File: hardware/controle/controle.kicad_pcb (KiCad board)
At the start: 2 copper layers, 97 x 67.8 mm, 79 parts, among them J1 Barrel_Jack, J10 Conn_01x05_Pin, J11 PWM, J12 ADC, J2 Serial, J3 PWR, J4 DATA, J5 UART7, J6 TWI3, J7 SENS0375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

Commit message: Controle: route board
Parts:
- moved R22 23.3 mm to (116.5, 90.0), turned to 0 degrees
- moved R21 23.2 mm to (111.6, 91.3), turned to 90 degrees
- moved R5 17.4 mm to (55.5, 91.0)
- moved R19 9.49 mm to (119.3, 105.2), turned to -90 degrees
- moved R4 9.22 mm to (50.9, 90.0), turned to 0 degrees
- moved C14 9.04 mm to (112.6, 102.7), turned to 90 degrees
- moved C15 6.83 mm to (119.3, 101.1), turned to 90 degrees
- moved C10 4.68 mm to (50.9, 86.0), turned to 0 degrees
- moved C4 3.36 mm to (82.9, 119.3)
- moved C5 3.36 mm to (93.1, 119.3)
- moved U2 3.36 mm to (89.7, 113.5)
- moved C3 3.36 mm to (84.1, 112.6)
- moved Y1 3.36 mm to (88.0, 120.6)
- moved J7 2.04 mm to (121.8, 120.0)
- moved R25 2.04 mm to (114.0, 123.5)
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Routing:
- net +3V3: track 0.00 -> 231.1 mm, vias 0 -> 4
- net +12V: track 0.00 -> 205.7 mm, vias 0 -> 2
- net GND: track 0.00 -> 115.2 mm, vias 0 -> 8
- net /power/+5VCPU: track 0.00 -> 103.0 mm, vias 0 -> 1
- net /PI2/TWI4_SCK: track 0.00 -> 84.0 mm
- net /PI3/TWI4_SDA: track 0.00 -> 73.7 mm
- net /PI15/EINT27: track 0.00 -> 57.2 mm, vias 0 -> 2
- net Net-(U3-VFB): track 0.00 -> 53.1 mm, vias 0 -> 2
- net Net-(D2-BK): track 0.00 -> 43.7 mm, vias 0 -> 1
- net /PI0/TWI3_SCK: track 0.00 -> 42.8 mm, vias 0 -> 2
- net Net-(D3-GK): track 0.00 -> 39.2 mm, vias 0 -> 1
- net Net-(D2-RK): track 0.00 -> 38.2 mm, vias 0 -> 1
- net /PI1/TWI3_SDA: track 0.00 -> 37.4 mm, vias 0 -> 2
- net Net-(D3-BK): track 0.00 -> 35.8 mm, vias 0 -> 1
- net /LIN/LBUS: track 0.00 -> 34.3 mm
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- added copper zone on B.Cu, net GND
- added copper zone on F.Cu, net GND

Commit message: Update LED resistors values. Minor updates to PCB
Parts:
- R10, R11, R12, R13, R14, R15, R16, R17, R18, R7, R8, R9: value 2.2K -> 330
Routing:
- net GND: track 115.2 -> 124.6 mm
- net /PI3/TWI4_SDA: track 73.7 -> 74.6 mm
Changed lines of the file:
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@@
 			)
 		)
-		(property "Value" "2.2K"
+		(property "Value" "330"
 			(at 0 1.65 0)
 			(layer "F.Fab")
@@
 			)
 		)
-		(property "Value" "2.2K"
+		(property "Value" "330"
 			(at 0 1.65 0)
 			(layer "F.Fab")
@@
 			)
 		)
-		(property "Value" "2.2K"
+		(property "Value" "330"
 			(at 0 1.65 0)
 			(layer "F.Fab")
@@
 			)
 		)
-		(property "Value" "2.2K"
+		(property "Value" "330"
 			(at 0 1.65 0)
 			(layer "F.Fab")
@@
 		(sheetname "Root")
 		(sheetfile "controle.kicad_sch")
-		(attr smd)
+		(attr smd dnp)
 		(fp_line
 			(start -0.227064 -0.735)
@@
 			)
 		)
-		(property "Value" "2.2K"
+		(property "Value" "330"
 			(at 0 1.65 0)
 			(layer "F.Fab")
@@
 			)
 		)
-		(property "Value" "2.2K"
+		(property "Value" "330"
 			(at 0 1.65 0)
 			(layer "F.Fab")
@@
 		(sheetname "Root")
 		(sheetfile "controle.kicad_sch")
-		(attr smd)
+		(attr smd dnp)
 		(fp_line
 			(start -0.227064 -0.735)
@@
 			)
 		)
-		(property "Value" "2.2K"
+		(property "Value" "330"
 			(at 0 1.65 0)
 			(layer "F.Fab")
@@
 		(sheetname "Root")
 		(sheetfile "controle.kicad_sch")
-		(attr smd)
+		(attr smd dnp)
 		(fp_line
 			(start -0.227064 -0.735)
@@
 			)
 		)
-		(property "Value" "2.2K"
+		(property "Value" "330"
 			(at 0 1.65 0)
 			(layer "F.Fab")
@@
 		(sheetname "Root")
 		(sheetfile "controle.kicad_sch")
-		(attr smd)
+		(attr smd dnp)
 		(fp_line
 			(start -0.227064 -0.735)
@@
 			)
 		)
-		(property "Value" "2.2K"
+		(property "Value" "330"
 			(at 0 1.65 0)
 			(layer "F.Fab")
@@
 		(sheetname "Root")
 		(sheetfile "controle.kicad_sch")
-		(attr smd)
+		(attr smd dnp)
 		(fp_line
 			(start -0.227064 -0.735)
@@
 		(tags "resistor handsolder")
 		(property "Reference" "R22"
-			(at 0 -1.65 360)
+			(at 0 -1.65 0)
 			(layer "F.SilkS")
 			(effects
@@
 		)
 		(property "Value" "10K"
-			(at 0 1.65 360)
+			(at 0 1.65 0)
 			(layer "F.Fab")
 			(effects
@@
 		)
 		(fp_text user "${REFERENCE}"
-			(at 0 0 360)
+			(at 0 0 0)
 			(layer "F.Fab")
 			(effects
@@
 		(tags "SOT TO_SOT_SMD")
 		(property "Reference" "Q1"
-			(at 0 -2.4 360)
+			(at 0 -2.4 0)
 			(layer "F.SilkS")
 			(effects
@@
 		)
 		(property "Value" "DMG2307L"
-			(at 0 2.4 360)
+			(at 0 2.4 0)
 			(layer "F.Fab")
 			(effects
@@
 		)
 		(fp_text user "${REFERENCE}"
-			(at 0 0 360)
+			(at 0 0 0)
 			(layer "F.Fab")
 			(effects
@@
 			)
 		)
-		(property "Value" "2.2K"
+		(property "Value" "330"
 			(at 0 1.65 0)
 			(layer "F.Fab")
@@
 			)
 		)
-		(property "Value" "2.2K"
+		(property "Value" "330"
 			(at 0 1.65 0)
 			(layer "F.Fab")
@@
 			)
 		)
-		(property "Value" "2.2K"
+		(property "Value" "330"
 			(at 0 1.65 0)
 			(layer "F.Fab")
@@
 		(sheetname "Root")
 		(sheetfile "controle.kicad_sch")
-		(attr smd)
+		(attr smd dnp)
 		(fp_line
 			(start -0.227064 -0.735)
@@
 	)
 	(segment
+		(start 105.918 103.8084)
+		(end 105.9324 103.8228)
+		(width 0.2)
+		(layer "F.Cu")
+		(net 2)
+	)
+	(segment
 		(start 103.6828 90.932)
 		(end 103.6828 89.679118)
@@
 	)
 	(segment
+		(start 105.918 103.8084)
+		(end 102.1856 103.8084)
+		(width 0.2)
+		(layer "F.Cu")
+		(net 2)
+	)
+	(segment
 		(start 103.6828 93.0556)
 		(end 103.6828 90.932)
@@
 	)
 	(segment
-		(start 109.1424 103.8084)
-		(end 102.1856 103.8084)
+		(start 105.9324 106.9484)
+		(end 110.363 111.379)
 		(width 0.2)
 		(layer "F.Cu")
@@
 	)
 	(segment
+		(start 109.1424 103.8084)
+		(end 105.918 103.8084)
+		(width 0.2)
+		(layer "F.Cu")
+		(net 2)
+	)
+	(segment
 		(start 92.3438 93.679348)
 		(end 93.599 92.424148)
@@
 		(net 2)
 	)
+	(segment
+		(start 105.9324 103.8228)
+		(end 105.9324 106.9484)
+		(width 0.2)
+		(layer "F.Cu")
+		(net 2)
+	)
 	(via
 		(at 124.968 125.222)
@@
 	(segment
 		(start 104.0624 105.5784)
-		(end 104.0624 106.553399)
+		(end 104.0624 106.2214)
 		(width 0.5)
 		(layer "F.Cu")
@@
 	)
 	(segment
-		(start 102.01 112.551)
-		(end 102.01 119.966001)
+		(start 89.764 100.305)
+		(end 100.203 110.744)
 		(width 0.5)
 		(layer "F.Cu")
@@
 	)
 	(segment
-		(start 124.3584 120.576799)
-		(end 122.405599 122.5296)
+		(start 104.0624 106.2214)
+		(end 115.316 117.475)
 		(width 0.5)
 		(layer "F.Cu")
@@
 	)
 	(segment
-		(start 89.764 100.305)
-		(end 102.01 112.551)
+		(start 100.203 118.159001)
+		(end 104.624399 122.5804)
 		(width 0.5)
 		(layer "F.Cu")
@@
 	)
 	(segment
-		(start 102.01 119.966001)
-		(end 104.624399 122.5804)
+		(start 100.203 110.744)
+		(end 100.203 118.159001)
+		(width 0.5)
+		(layer "F.Cu")
+		(net 52)
+	)
+	(segment
+		(start 104.624399 122.5804)
+		(end 105.945199 122.5804)
 		(width 0.5)
 		(layer "F.Cu")
@@
 	)
 	(segment
-		(start 104.624399 122.5804)
-		(end 105.945199 122.5804)
-		(width 0.5)
+		(start 114.022399 122.5296)
+		(end 105.995999 122.5296)
+		(width 0.4)
 		(layer "F.Cu")
 		(net 52)
 	)
 	(segment
-		(start 104.0624 106.553399)
-		(end 114.984001 117.475)
+		(start 124.3584 120.576799)
+		(end 122.405599 122.5296)
 		(width 0.5)
 		(layer "F.Cu")
@@
 	)
 	(segment
-		(start 114.022399 122.5296)
-		(end 105.995999 122.5296)
-		(width 0.4)
+		(start 115.316 117.475)
+		(end 122.430999 117.475)
+		(width 0.5)
 		(layer "F.Cu")
 		(net 52)
@@
 	)
 	(segment
-		(start 114.984001 117.475)
-		(end 122.430999 117.475)
-		(width 0.5)
-		(layer "F.Cu")
-		(net 52)
-	)
-	(segment
 		(start 67.3404 88.2824)
 		(end 66.2004 87.1424)
@@
 	)
 	(segment
-		(start 116.332 120.0404)
-		(end 102.7924 106.5008)
+		(start 90.399 99.035)
+		(end 101.219 109.855)
 		(width 0.5)
 		(layer "F.Cu")
@@
 	)
 	(segment
-		(start 81.837 99.035)
-		(end 90.399 99.035)
+		(start 102.7924 106.136084)
+		(end 102.7924 105.5784)
+		(width 0.5)
+		(layer "F.Cu")
+		(net 56)
+	)
+	(segment
+		(start 104.1654 120.0404)
+		(end 105.945199 120.0404)
 		(width 0.5)
 		(layer "F.Cu")
@@
 	)
 	(segment
-		(start 102.71 111.346)
-		(end 102.71 114.109138)
+		(start 116.586 120.0404)
+		(end 116.586 119.929684)
 		(width 0.5)
 		(layer "F.Cu")
@@
 	)
 	(segment
-		(start 116.586 120.0404)
-		(end 116.332 120.0404)
+		(start 81.837 99.035)
+		(end 90.399 99.035)
 		(width 0.5)
 		(layer "F.Cu")
@@
 	)
 	(segment
-		(start 102.7924 106.5008)
-		(end 102.7924 105.5784)
+		(start 101.219 109.855)
+		(end 101.219 117.094)
 		(width 0.5)
 		(layer "F.Cu")
@@
 	)
 	(segment
-		(start 117.730799 120.0912)
-		(end 117.679999 120.0404)
+		(start 116.586 119.929684)
+		(end 102.7924 106.136084)
 		(width 0.5)
 		(layer "F.Cu")
@@
 	)
 	(segment
-		(start 102.71 114.109138)
-		(end 105.945199 117.344337)
+		(start 117.730799 120.0912)
+		(end 117.679999 120.0404)
 		(width 0.5)
 		(layer "F.Cu")
@@
 	)
 	(segment
-		(start 105.945199 117.344337)
-		(end 105.945199 120.0404)
+		(start 101.219 117.094)
+		(end 104.1654 120.0404)
 		(width 0.5)
 		(layer "F.Cu")
@@
 		(width 0.5)
 		(layer "F.Cu")
-		(net 56)
-	)
-	(segment
-		(start 90.399 99.035)
-		(end 102.71 111.346)
-		(width 0.5)
-		(layer "F.Cu")

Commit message: controle: minor board update
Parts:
- moved R6 1.98 mm to (115.4, 70.8), turned to -90 degrees
- moved D1 1.81 mm to (111.6, 71.8), turned to -90 degrees
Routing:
- net /LIN/LBUS: track 34.3 -> 30.7 mm

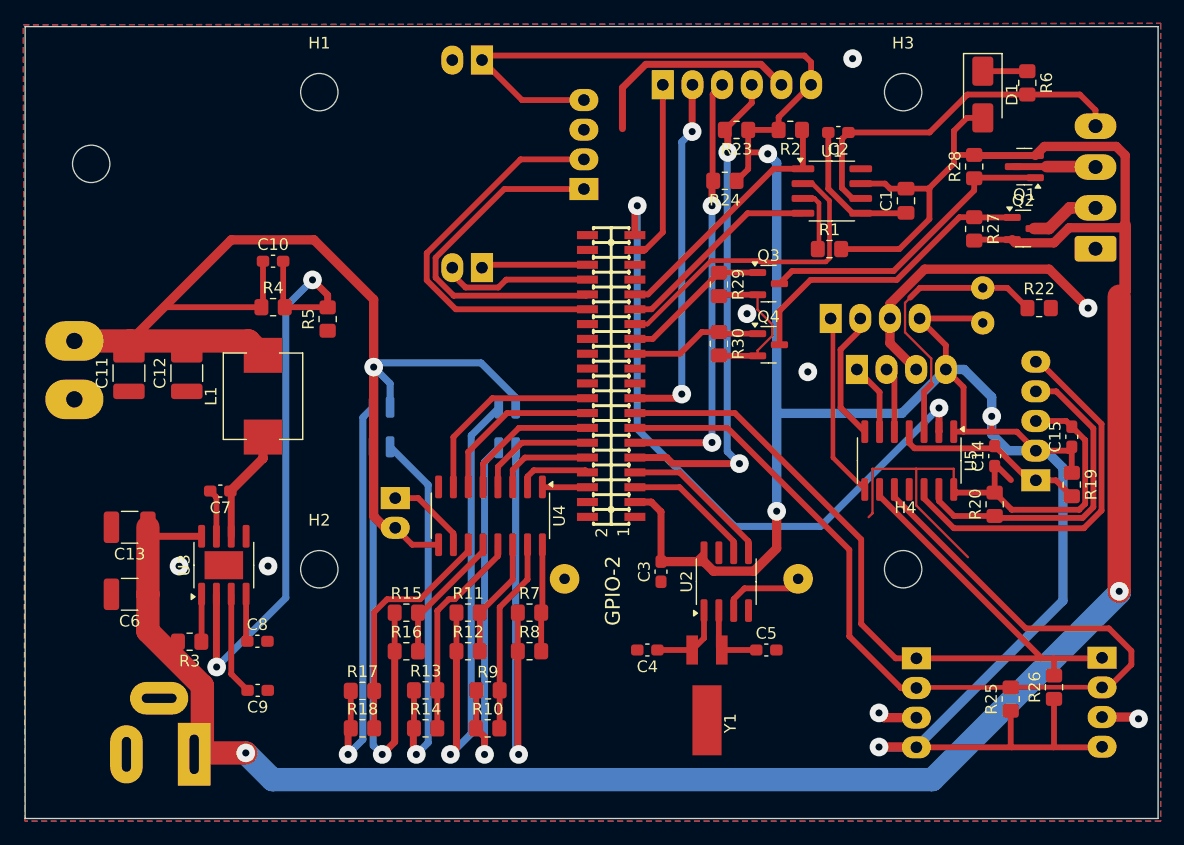
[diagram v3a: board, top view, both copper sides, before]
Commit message: controle: - add leds for LIN power - add optional led for LIN activity - fix lime2 mounting holes - other misc cleanups
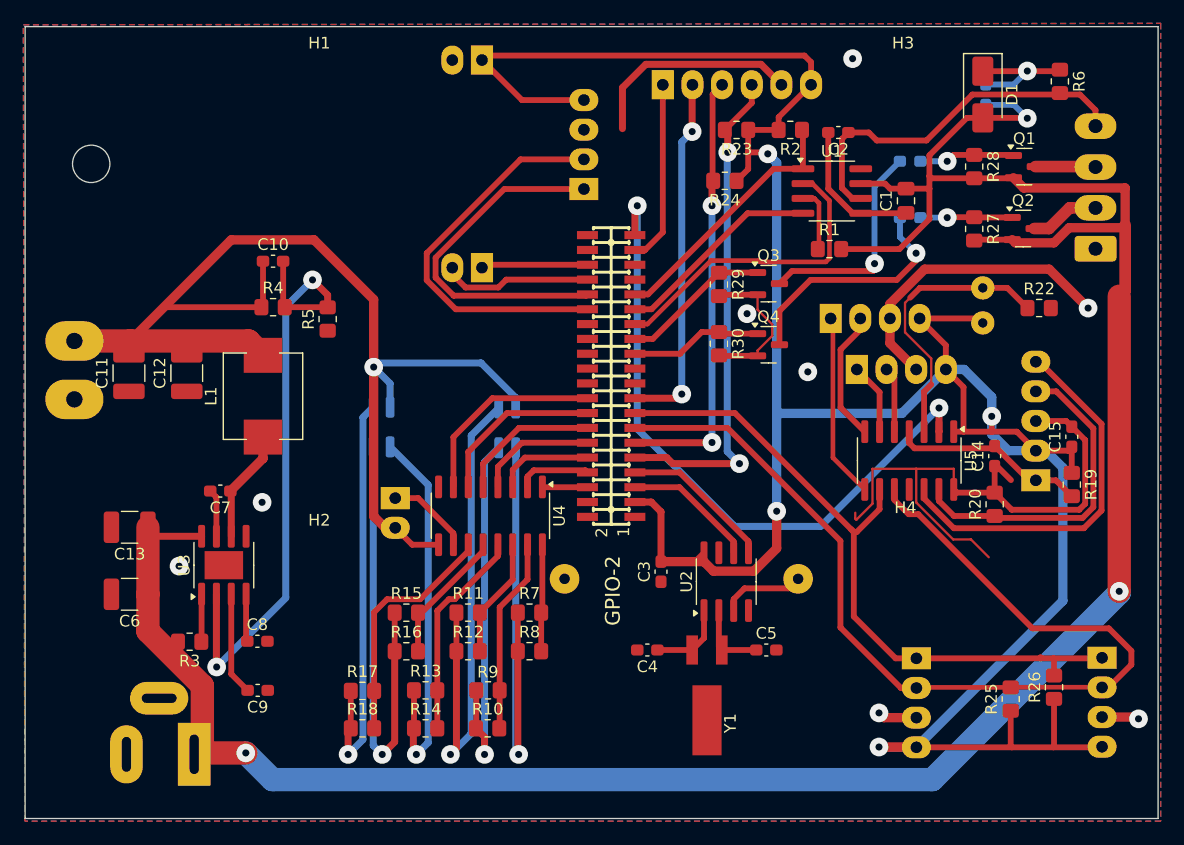
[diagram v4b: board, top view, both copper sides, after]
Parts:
- added D4: RED, LED_SMD:LED_0603_1608Metric_Pad1.05x0.95mm_HandSolder, B.Cu at (105.4, 77.5)
- added D5: RED, LED_SMD:LED_0603_1608Metric_Pad1.05x0.95mm_HandSolder, B.Cu at (105.4, 82.3)
- added D6: RED, LED_SMD:LED_0603_1608Metric_Pad1.05x0.95mm_HandSolder, B.Cu at (111.9, 71.8)
- R27, R28: value 47K -> 2.2K
- moved R6 2.80 mm to (118.2, 70.6)
- turned Q1 to 0 degrees
- turned R28 to -90 degrees
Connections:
- Q1 pad 1: Net-(Q1-G) -> Net-(D4-A)
- Q2 pad 1: Net-(Q2-G) -> Net-(D5-A)
- Q3 pad 3: Net-(Q1-G) -> Net-(D4-K)
- Q4 pad 3: Net-(Q2-G) -> Net-(D5-K)
- R27 pad 1: Net-(Q2-G) -> Net-(D5-A)
- R28 pad 1: Net-(Q1-G) -> Net-(D4-A)
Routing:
- net Net-(Q1-G): track 26.2 -> 0.00 mm
- net Net-(Q2-G): track 26.1 -> 0.00 mm
- net Net-(D5-K): track 0.00 -> 20.6 mm, vias 0 -> 1
- net Net-(D4-K): track 0.00 -> 18.8 mm, vias 0 -> 1
- net /PI3/TWI4_SDA: track 74.6 -> 59.6 mm
- net Net-(D4-A): track 0.00 -> 8.14 mm, vias 0 -> 1
- net Net-(D5-A): track 0.00 -> 7.86 mm, vias 0 -> 1
- net +12V: track 205.8 -> 212.8 mm, vias 2 -> 3
- net Net-(D1-K): track 3.81 -> 10.5 mm, vias 0 -> 1
- net GND: track 124.6 -> 127.5 mm
- net /LIN/+12V1: track 7.00 -> 5.12 mm
- net /LIN/LBUS: track 30.7 -> 31.2 mm

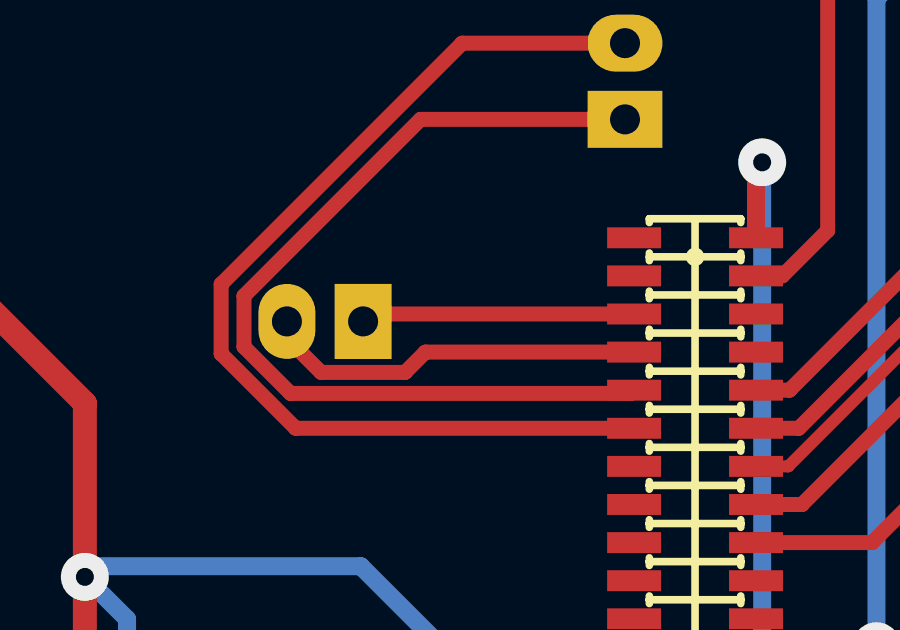
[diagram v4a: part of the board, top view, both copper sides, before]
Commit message: controle: fix orioentation of rs232 module connector
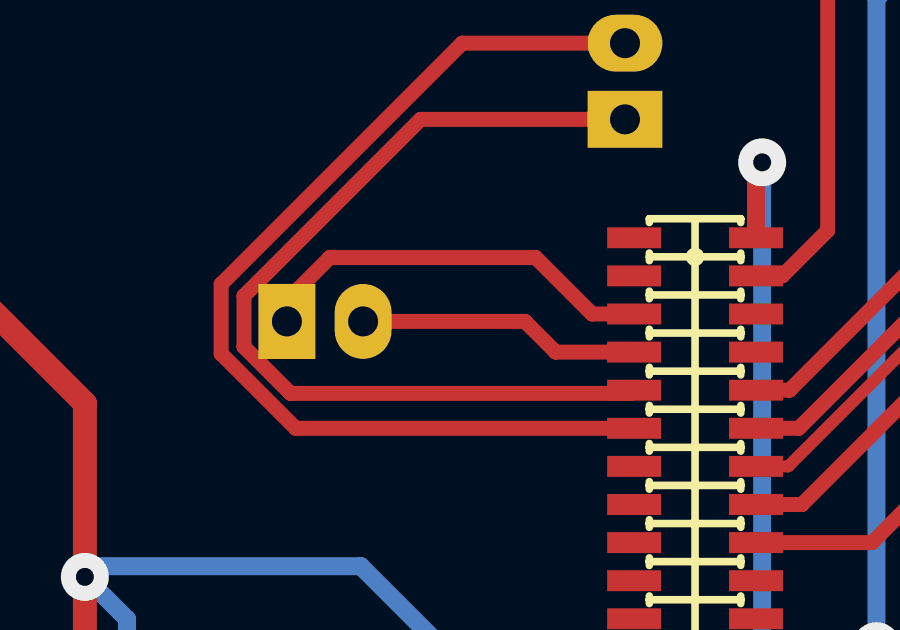
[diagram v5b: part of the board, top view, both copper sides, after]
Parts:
- moved J4 2.54 mm to (66.2, 86.6), turned to -90 degrees
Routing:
- net /PI18/UART2_TX: track 8.79 -> 13.6 mm
- net /PI19/UART2_RX: track 12.3 -> 9.46 mm
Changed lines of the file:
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@@
 		(tags "SOT TO_SOT_SMD")
 		(property "Reference" "Q1"
-			(at 0 -2.4 360)
+			(at 0 -2.4 0)
 			(layer "F.SilkS")
 			(effects
@@
 		)
 		(property "Value" "DMG2307L"
-			(at 0 2.4 360)
+			(at 0 2.4 0)
 			(layer "F.Fab")
 			(effects
@@
 		)
 		(fp_text user "${REFERENCE}"
-			(at 0 0 360)
+			(at 0 0 0)
 			(layer "F.Fab")
 			(effects
@@
 		(tags "LED handsolder")
 		(property "Reference" "D4"
-			(at 0 1.43 360)
+			(at 0 1.43 0)
 			(layer "B.SilkS")
 			(effects
@@
 		)
 		(property "Value" "RED"
-			(at 0 -1.43 360)
+			(at 0 -1.43 0)
 			(layer "B.Fab")
 			(effects
@@
 		)
 		(fp_text user "${REFERENCE}"
-			(at 0 0 360)
+			(at 0 0 0)
 			(layer "B.Fab")
 			(effects
@@
 	(footprint "Connector_PinSocket_2.54mm:PinSocket_1x02_P2.54mm_Vertical"
 		(layer "B.Cu")
-		(at 68.7404 86.5824 90)
+		(at 66.2004 86.5824 -90)
 		(descr "Through hole straight socket strip, 1x02, 2.54mm pitch, single row (from Kicad 4.0.7), script generated")
 		(tags "Through hole socket strip THT 1x02 2.54mm single row")
@@
 		)
 		(property "Footprint" "Connector_PinSocket_2.54mm:PinSocket_1x02_P2.54mm_Vertical"
-			(at 0 0 -90)
+			(at 0 0 90)
 			(unlocked yes)
 			(layer "B.Fab")
@@
 		)
 		(property "Datasheet" ""
-			(at 0 0 -90)
+			(at 0 0 90)
 			(unlocked yes)
 			(layer "B.Fab")
@@
 		)
 		(property "Description" "Generic connector, single row, 01x02, script generated"
-			(at 0 0 -90)
+			(at 0 0 90)
 			(unlocked yes)
 			(layer "B.Fab")
@@
 		)
 		(property "P/N" ""
-			(at 0 0 -90)
+			(at 0 0 90)
 			(unlocked yes)
 			(layer "B.Fab")
@@
 		(attr through_hole)
 		(fp_line
-			(start 1.33 -3.87)
-			(end -1.33 -3.87)
+			(start 1.33 1.33)
+			(end 0 1.33)
 			(stroke
 				(width 0.12)
@@
 		)
 		(fp_line
-			(start 1.33 -3.87)
-			(end 1.33 -1.27)
+			(start 1.33 0)
+			(end 1.33 1.33)
 			(stroke
 				(width 0.12)
@@
 		)
 		(fp_line
-			(start -1.33 -3.87)
+			(start 1.33 -1.27)
 			(end -1.33 -1.27)
 			(stroke
@@
 		)
 		(fp_line
-			(start 1.33 -1.27)
+			(start -1.33 -3.87)
 			(end -1.33 -1.27)
 			(stroke
@@
 		)
 		(fp_line
-			(start 1.33 0)
-			(end 1.33 1.33)
+			(start 1.33 -3.87)
+			(end 1.33 -1.27)
 			(stroke
 				(width 0.12)
@@
 		)
 		(fp_line
-			(start 1.33 1.33)
-			(end 0 1.33)
+			(start 1.33 -3.87)
+			(end -1.33 -3.87)
 			(stroke
 				(width 0.12)
@@
 		)
 		(fp_line
-			(start 1.75 -4.3)
-			(end 1.75 1.8)
+			(start -1.8 1.8)
+			(end -1.8 -4.3)
 			(stroke
 				(width 0.05)
@@
 		)
 		(fp_line
-			(start -1.8 -4.3)
-			(end 1.75 -4.3)
+			(start 1.75 1.8)
+			(end -1.8 1.8)
 			(stroke
 				(width 0.05)
@@
 		)
 		(fp_line
-			(start 1.75 1.8)
-			(end -1.8 1.8)
+			(start -1.8 -4.3)
+			(end 1.75 -4.3)
 			(stroke
 				(width 0.05)
@@
 		)
 		(fp_line
-			(start -1.8 1.8)
-			(end -1.8 -4.3)
+			(start 1.75 -4.3)
+			(end 1.75 1.8)
 			(stroke
 				(width 0.05)
@@
 		)
 		(fp_line
-			(start 1.27 -3.81)
-			(end 1.27 0.635)
+			(start -1.27 1.27)
+			(end -1.27 -3.81)
 			(stroke
 				(width 0.1)
@@
 		)
 		(fp_line
-			(start -1.27 -3.81)
-			(end 1.27 -3.81)
+			(start 0.635 1.27)
+			(end -1.27 1.27)
 			(stroke
 				(width 0.1)
@@
 		)
 		(fp_line
-			(start 0.635 1.27)
-			(end -1.27 1.27)
+			(start -1.27 -3.81)
+			(end 1.27 -3.81)
 			(stroke
 				(width 0.1)
@@
 		)
 		(fp_line
-			(start -1.27 1.27)
-			(end -1.27 -3.81)
+			(start 1.27 -3.81)
+			(end 1.27 0.635)
 			(stroke
 				(width 0.1)
@@
 		)
 		(pad "1" thru_hole rect
-			(at 0 0 90)
+			(at 0 0 270)
 			(size 2.5 1.9)
 			(drill 1)
@@
 		)
 		(pad "2" thru_hole oval
-			(at 0 -2.54 90)
+			(at 0 -2.54 270)
 			(size 2.5 1.9)
 			(drill 1)
@@
 		(tags "LED handsolder")
 		(property "Reference" "D5"
-			(at 0 1.43 360)
+			(at 0 1.43 0)
 			(layer "B.SilkS")
 			(effects
@@
 		)
 		(property "Value" "RED"
-			(at 0 -1.43 360)
+			(at 0 -1.43 0)
 			(layer "B.Fab")
 			(effects
@@
 		)
 		(fp_text user "${REFERENCE}"
-			(at 0 0 360)
+			(at 0 0 0)
 			(layer "B.Fab")
 			(effects
@@
 	)
 	(segment
-		(start 67.3404 88.2824)
-		(end 66.2004 87.1424)
+		(start 75.159 87.605)
+		(end 74.1364 86.5824)
 		(width 0.5)
 		(layer "F.Cu")
@@
 	)
 	(segment
-		(start 70.8178 87.605)
-		(end 70.1404 88.2824)
+		(start 74.1364 86.5824)
+		(end 68.7404 86.5824)
 		(width 0.5)
 		(layer "F.Cu")
@@
 	(segment
 		(start 77.773 87.605)
-		(end 70.8178 87.605)
+		(end 75.159 87.605)
 		(width 0.5)
 		(layer "F.Cu")
@@
 	)
 	(segment
-		(start 70.1404 88.2824)
-		(end 67.3404 88.2824)
+		(start 66.2004 85.883)
+		(end 66.2004 86.5824)
 		(width 0.5)
 		(layer "F.Cu")
-		(net 53)
+		(net 54)
+	)
+	(segment
+		(start 76.37384 86.335)
+		(end 74.49384 84.455)
+		(width 0.5)
+		(layer "F.Cu")
+		(net 54)
+	)
+	(segment
+		(start 67.6284 84.455)
+		(end 66.2004 85.883)
+		(width 0.5)
+		(layer "F.Cu")
+		(net 54)
 	)
 	(segment
 		(start 77.773 86.335)
-		(end 68.9878 86.335)
+		(end 76.37384 86.335)
+		(width 0.5)
+		(layer "F.Cu")
+		(net 54)
+	)
+	(segment
+		(start 74.49384 84.455)
+		(end 67.6284 84.455)
 		(width 0.5)
 		(layer "F.Cu")
